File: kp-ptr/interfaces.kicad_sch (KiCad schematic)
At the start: 20 parts, among them IC2 E22-900M22S, J4 USB_C_Receptacle_USB2.0, J5 u.fl, U11 USBLC6-2SC6, U12 NL27WZU04DBVT1G, U13 W25Q256

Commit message: Wersja produkcyjna v1
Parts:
- D9: value LED -> BLUE
- FB2: value 1000mA -> GZ1608D601TF
- U12: footprint KP-PTR_lib:SOT95P275X110-6N -> Package_TO_SOT_SMD:SOT-363_SC-70-6
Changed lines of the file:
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@@
     (property "Reference" "U12" (id 0) (at 184.15 59.69 0))
     (property "Value" "NL27WZU04DBVT1G" (id 1) (at 180.34 69.85 0))
-    (property "Footprint" "KP-PTR_lib:SOT95P275X110-6N" (id 2) (at 179.07 73.66 0)
+    (property "Footprint" "Package_TO_SOT_SMD:SOT-363_SC-70-6" (id 2) (at 179.07 73.66 0)
       (effects (font (size 1.27 1.27)) hide)
     )
@@
       (effects (font (size 1.27 1.27)) (justify left))
     )
-    (property "Value" "1000mA" (id 1) (at 179.07 26.67 90)
+    (property "Value" "GZ1608D601TF" (id 1) (at 182.245 26.67 90)
       (effects (font (size 1.27 1.27)) (justify left))
     )
@@
       (effects (font (size 1.27 1.27)) (justify right))
     )
-    (property "Value" "LED" (id 1) (at 161.29 60.6424 90)
+    (property "Value" "BLUE" (id 1) (at 161.29 60.6424 90)
       (effects (font (size 1.27 1.27)) (justify right))
     )

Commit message: Release v1
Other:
- company: (none) -> Polskie Towarzystwo Rakietowe
- title: (none) -> KP-PTR
- moved on the sheet: C46, C47, C48, C49, C50, D8, D9, FB2, IC2, J4, J5, R36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

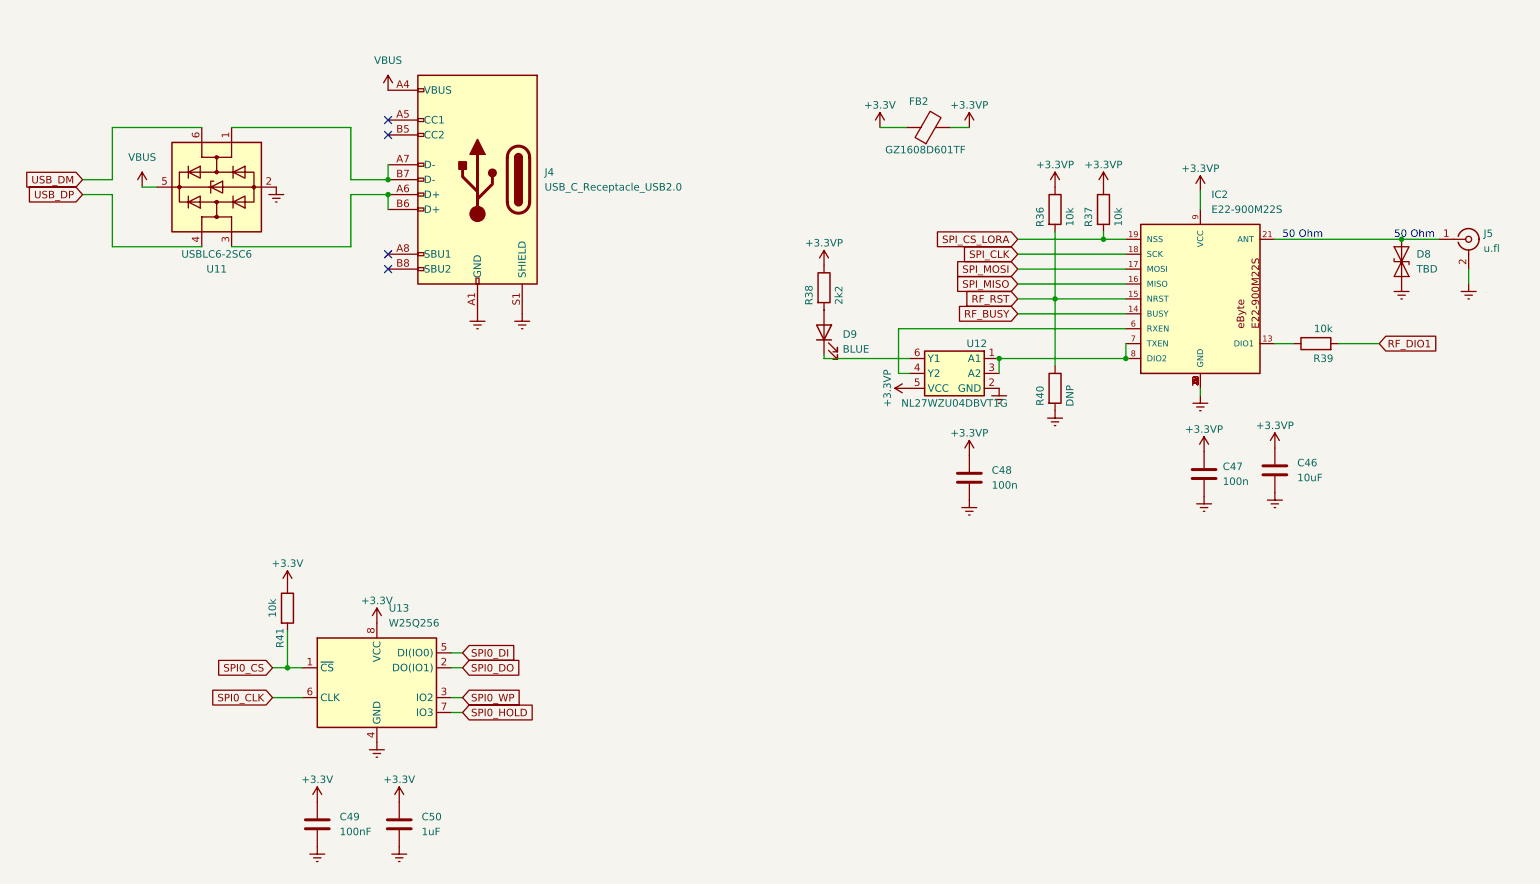
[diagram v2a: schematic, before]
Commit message: New schematic revision v1.1:
- added 'DNP' info for few components
- some stylistic improvements
- added comment about I2C pins glitch
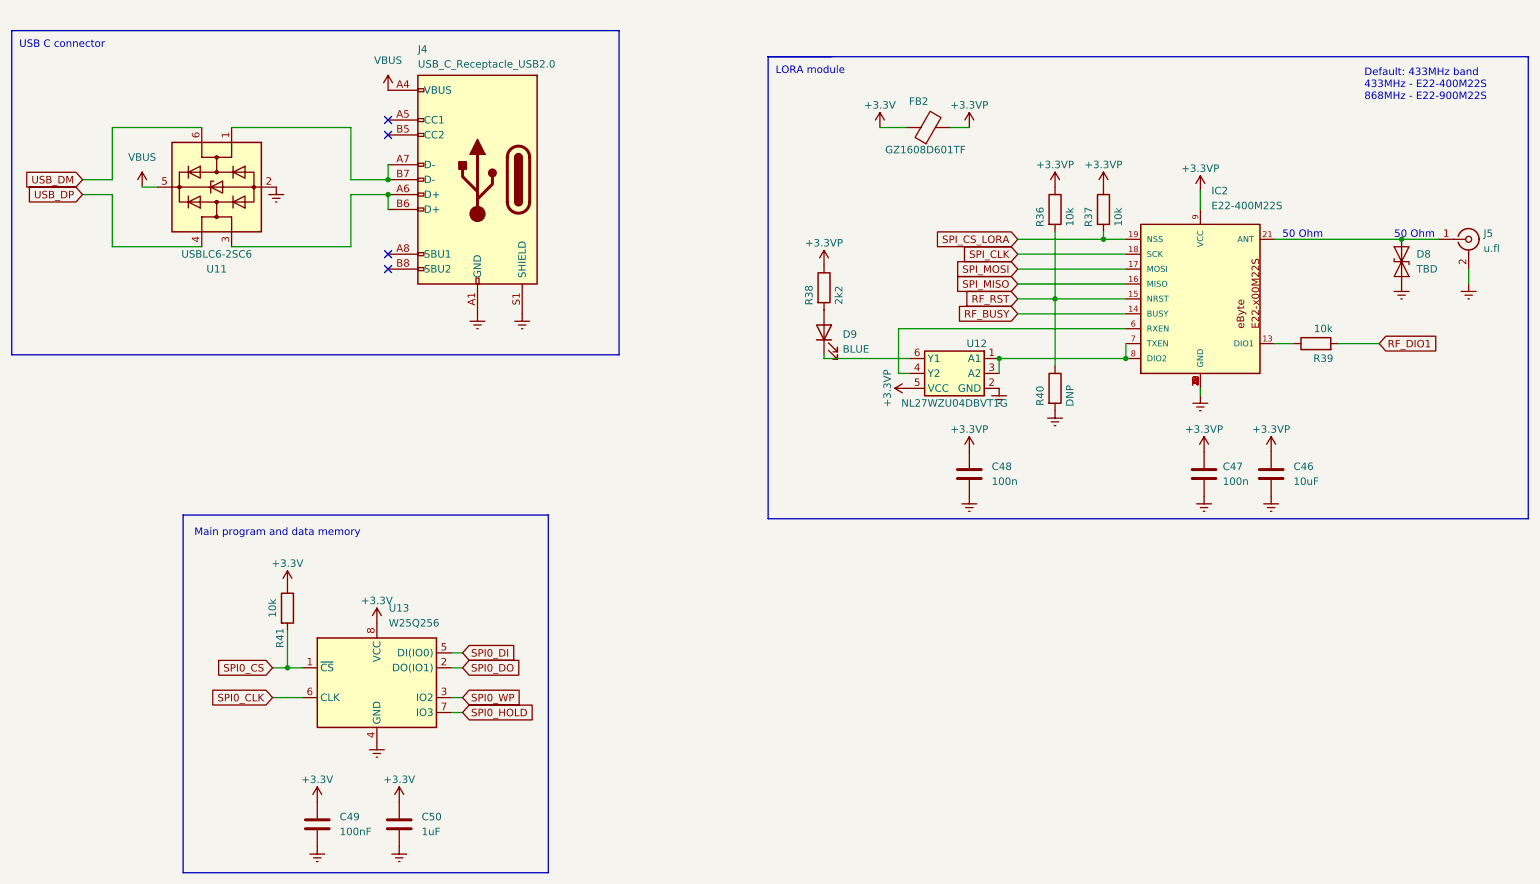
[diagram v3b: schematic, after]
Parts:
- IC2: value E22-900M22S -> E22-400M22S
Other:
- note added: "Default: 433MHz band 433MHz - E22-400M22S 868MHz - E22-900M22S"
- note added: "LORA module"
- note added: "Main program and data memory"
- note added: "USB C connector"
- moved on the sheet: C46, C48

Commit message: + Kicad update to 9.0
+ CC resistors added
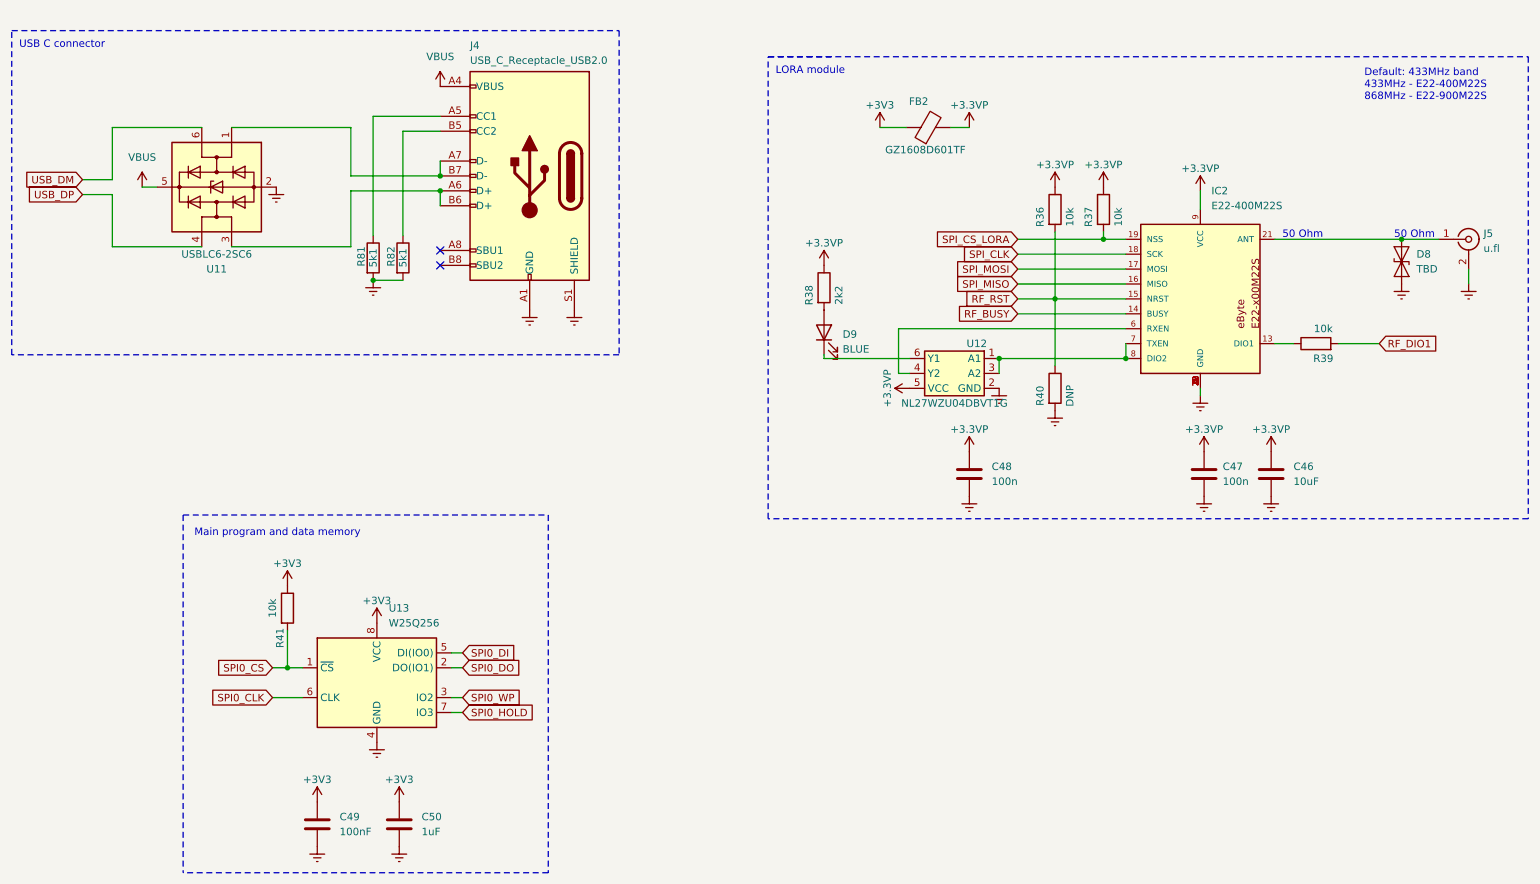
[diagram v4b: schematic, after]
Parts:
- added R81, R82: 5k1, Resistor_SMD:R_0402_1005Metric, symbol Device:R
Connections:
- net Earth: now also R81.2, R82.2
- net at J4.A5 (CC1): now also R81.1
- net at J4.B5 (CC2): now also R82.1
- no-connect marks 4 -> 2
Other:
- moved on the sheet: J4
